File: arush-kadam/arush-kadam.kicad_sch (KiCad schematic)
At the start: 8 parts, among them IC1 AP63301WU-7

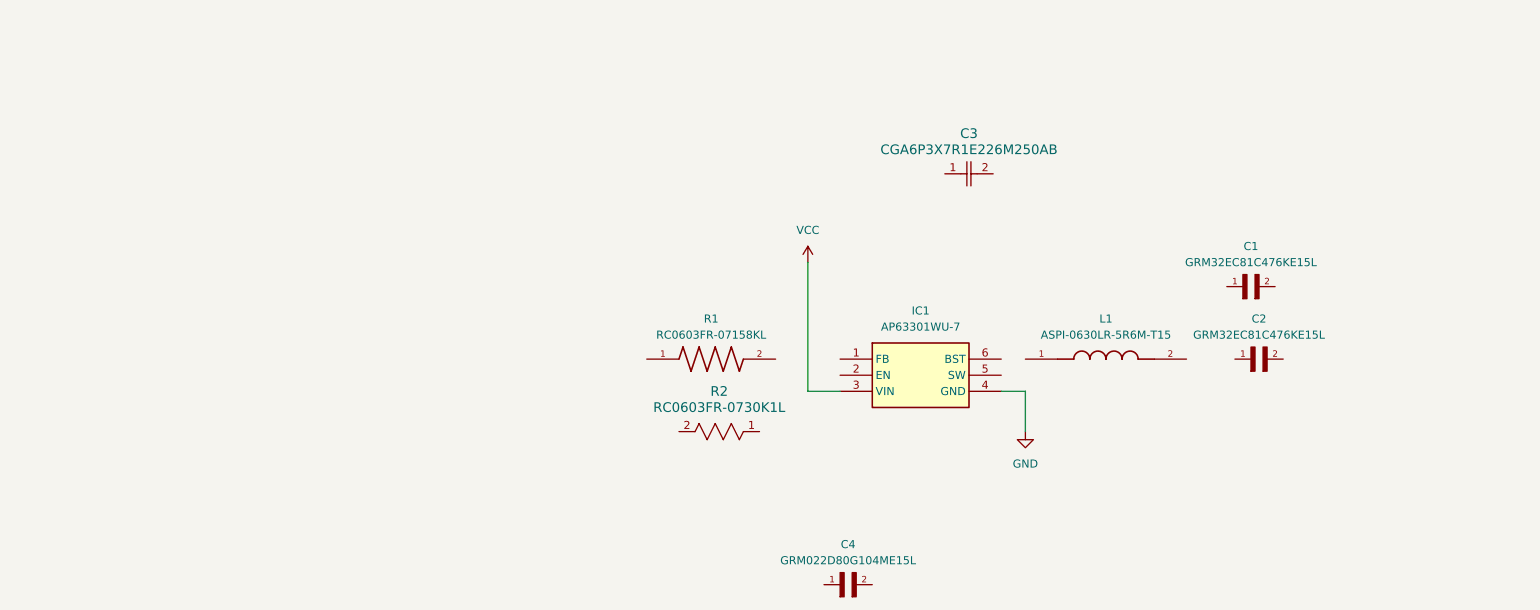
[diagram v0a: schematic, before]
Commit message: Replaced components with manufactured recommended values
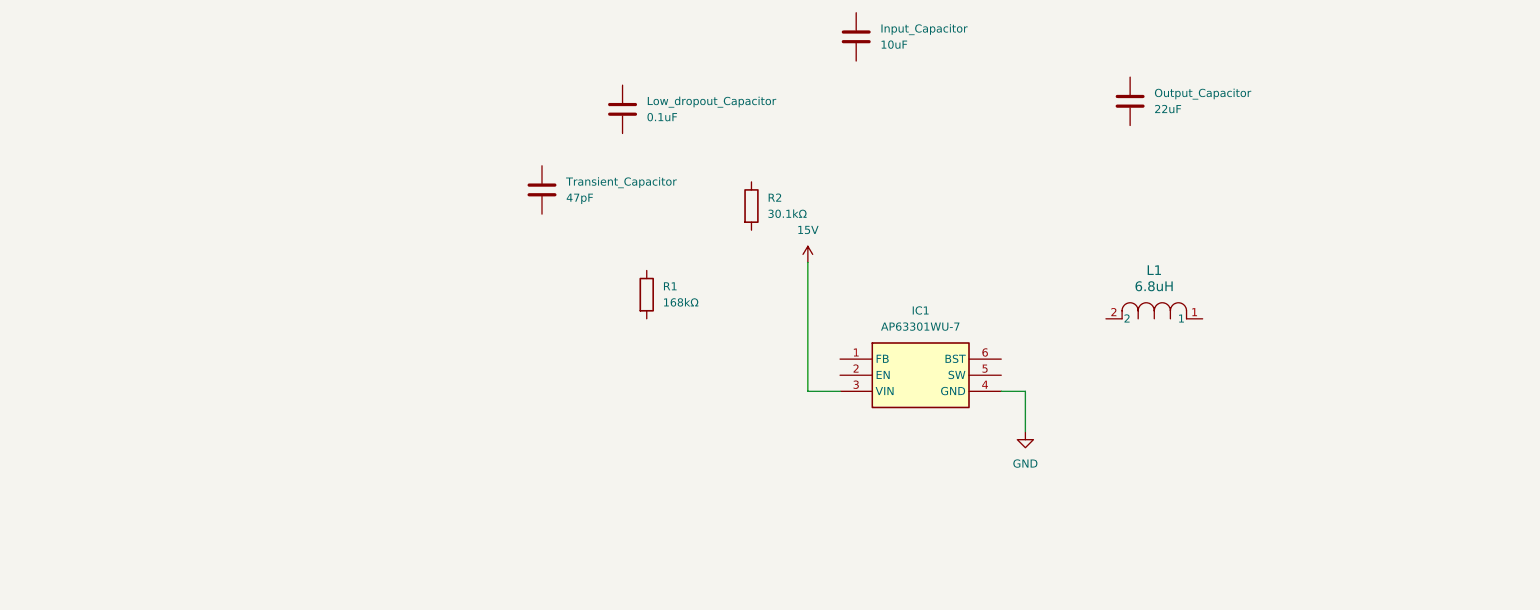
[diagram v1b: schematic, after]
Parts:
- removed C1, C2: GRM32EC81C476KE15L, GRM32EC81C476KE15L:CAPC3225X270N, symbol GRM32EC81C476KE15L:GRM32EC81C476KE15L
- removed C3: CGA6P3X7R1E226M250AB, CAP_CGA6_TDK, symbol 2026-10-15_08-26-09:CGA6P3X7R1E226M250AB
- removed C4: GRM022D80G104ME15L, GRM022D80G104ME15L:CAPC0402X22N, symbol GRM022D80G104ME15L:GRM022D80G104ME15L
- removed L1: ASPI-0630LR-5R6M-T15, ASPI-0630LR-5R6M-T15:IND_ASPI-0630LR-5R6M-T15, symbol ASPI-0630LR-5R6M-T15:ASPI-0630LR-5R6M-T15
- removed R1: RC0603FR-07158KL, RC0603FR-07158KL:RESC1608X55N, symbol RC0603FR-07158KL:RC0603FR-07158KL
- removed R2: RC0603FR-0730K1L, RC0603N_YAG, symbol 2026-10-15_00-52-59:RC0603FR-0730K1L
- added Input_Capacitor: 10uF, Capacitor_SMD:C_0805_2012Metric, symbol Device:C
- added L1: 6.8uH, IND_SRN8040TA-6R8M_BRN, symbol 2026-10-16_19-50-59:SRN8040TA-6R8M
- added Low_dropout_Capacitor: 0.1uF, Capacitor_SMD:C_0603_1608Metric_Pad1.05x0.95mm_HandSolder, symbol Device:C
- added Output_Capacitor: 22uF, Capacitor_SMD:C_0805_2012Metric, symbol Device:C
- added R1: 168kΩ, Resistor_SMD:R_0603_1608Metric_Pad0.98x0.95mm_HandSolder, symbol Device:R
- added R2: 30.1kΩ, Resistor_SMD:R_0603_1608Metric_Pad0.98x0.95mm_HandSolder, symbol Device:R
- added Transient_Capacitor: 47pF, Capacitor_SMD:C_0603_1608Metric_Pad1.05x0.95mm_HandSolder, symbol Device:C
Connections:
- net VCC renamed 15V

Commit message: Finished wiring schematic
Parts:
- removed Input_Capacitor: 10uF, Capacitor_SMD:C_0805_2012Metric, symbol Device:C
- removed Low_dropout_Capacitor: 0.1uF, Capacitor_SMD:C_0603_1608Metric_Pad1.05x0.95mm_HandSolder, symbol Device:C
- removed Output_Capacitor: 22uF, Capacitor_SMD:C_0805_2012Metric, symbol Device:C
- removed Transient_Capacitor: 47pF, Capacitor_SMD:C_0603_1608Metric_Pad1.05x0.95mm_HandSolder, symbol Device:C
- added C1 (x4): 10uF, Capacitor_SMD:C_0805_2012Metric, symbol Device:C
- added C2 (x7): 22uF, Capacitor_SMD:C_0805_2012Metric, symbol Device:C
- added C3: 0.1uF, Capacitor_SMD:C_0603_1608Metric_Pad1.05x0.95mm_HandSolder, symbol Device:C
- added C4: 47pF, Capacitor_SMD:C_0603_1608Metric_Pad1.05x0.95mm_HandSolder, symbol Device:C
- IC1: Digikey Part Number (none) -> 31-AP63301WU-7CT-ND; Digikey URL (none) -> https://www.digikey.com/en/products/detail/diodes-incorpora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
- L1: Digikey Part Number (none) -> SRN8040TA-6R8MCT-ND; Digikey URL (none) -> https://www.digikey.com/en/products/detail/bourns-inc/SRN80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; Manufacturer (none) -> Bourns Inc.
- R1: Digikey Part Number (none) -> 311-158KHRCT-ND; Digikey URL (none) -> https://www.digikey.com/en/products/detail/yageo/RC0603FR-0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; Manufacturer (none) -> YAGEO
- R2: Digikey Part Number (none) -> 311-30.1KHRCT-ND; Digikey URL (none) -> https://www.digikey.com/en/products/detail/yageo/RC0603FR-0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; Manufacturer (none) -> YAGEO
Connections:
- net 15V: now also IC1.2 (EN), C1.1, C1.1, C1.1, C1.1
- net GND: now also R2.2, C1.2, C1.2, C1.2, C1.2, C2.2, C2.2, C2.2, C2.2, C2.2, C2.2, C2.2
- net 5V: now reaches R1.1
- net 5V: now also L1.1, C2.1, C2.1, C2.1, C2.1, C2.1, C2.1, C2.1, C4.1
- net FB: now reaches R1.2
- net FB: now also IC1.1 (FB), R2.1, C4.2
- net SW: now reaches IC1.5 (SW)
- net SW: now also L1.2, C3.2
- net BST: now reaches IC1.6 (BST)
- net BST: now also C3.1

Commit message: Fixed resistor values and footprints
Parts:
- R1: value 168kΩ -> 158kΩ
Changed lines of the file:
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@@
+		)
+	)
+	(label "out"
+		(at 255.27 90.17 0)
+		(effects
+			(font
+				(size 1.27 1.27)
+			)
+			(justify left bottom)
 		)
 	)
@@
 	)
 	(label ""
+		(at 25.4 85.09 0)
+		(effects
+			(font
+				(size 1.27 1.27)
+			)
+			(justify left bottom)
+		)
+	)
+	(label "IN"
+		(at 25.4 85.09 0)
+		(effects
+			(font
+				(size 1.27 1.27)
+			)
+			(justify left bottom)
+		)
+	)
+	(label ""
 		(at 416.56 218.44 0)
 		(effects
@@
 		)
 	)
-	(label ""
-		(at 130.81 90.17 0)
+	(label "VIN"
+		(at 64.77 90.17 0)
 		(effects
 			(font
@@
 			)
 		)
-		(property "Value" "168kΩ"
+		(property "Value" "158kΩ"
 			(at 163.83 101.5999 0)
 			(show_name no)

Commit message: Added documentation PDF and fixed capacitor names on schematic
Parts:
- renumbered C2 to C10, C2 to C11, C2 to C12, C2 to C13, C1 to C2, C1 to C3, C1 to C4, C3 to C5, C4 to C6, C2 to C7, C2 to C8, C2 to C9
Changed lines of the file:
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@@
 		(in_pos_files yes)
 		(dnp no)
-		(property "Reference" "C4"
+		(property "Reference" "C6"
 			(at 142.494 100.584 0)
 			(show_name no)
@@
 			(project "arush-kadam"
 				(path "/e994741c-7c7d-4124-9d00-43b883baa61d"
-					(reference "C4")
+					(reference "C6")
 					(unit 1)
 				)
@@
 		(dnp no)
 		(fields_autoplaced yes)
-		(property "Reference" "C2"
+		(property "Reference" "C7"
 			(at 177.8 99.0599 0)
 			(show_name no)
@@
 			(project "arush-kadam"
 				(path "/e994741c-7c7d-4124-9d00-43b883baa61d"
-					(reference "C2")
+					(reference "C7")
 					(unit 1)
 				)
@@
 		(dnp no)
 		(fields_autoplaced yes)
-		(property "Reference" "C2"
+		(property "Reference" "C9"
 			(at 200.66 99.0599 0)
 			(show_name no)
@@
 			(project "arush-kadam"
 				(path "/e994741c-7c7d-4124-9d00-43b883baa61d"
-					(reference "C2")
+					(reference "C9")
 					(unit 1)
 				)
@@
 		(dnp no)
 		(fields_autoplaced yes)
-		(property "Reference" "C2"
+		(property "Reference" "C10"
 			(at 210.82 99.0599 0)
 			(show_name no)
@@
 			(project "arush-kadam"
 				(path "/e994741c-7c7d-4124-9d00-43b883baa61d"
-					(reference "C2")
+					(reference "C10")
 					(unit 1)
 				)
@@
 		(dnp no)
 		(fields_autoplaced yes)
-		(property "Reference" "C1"
+		(property "Reference" "C3"
 			(at 55.88 100.3299 0)
 			(show_name no)
@@
 			(project "arush-kadam"
 				(path "/e994741c-7c7d-4124-9d00-43b883baa61d"
-					(reference "C1")
+					(reference "C3")
 					(unit 1)
 				)
@@
 		(dnp no)
 		(fields_autoplaced yes)
-		(property "Reference" "C2"
+		(property "Reference" "C12"
 			(at 234.95 99.0599 0)
 			(show_name no)
@@
 			(project "arush-kadam"
 				(path "/e994741c-7c7d-4124-9d00-43b883baa61d"
-					(reference "C2")
+					(reference "C12")
 					(unit 1)
 				)
@@
 		(dnp no)
 		(fields_autoplaced yes)
-		(property "Reference" "C3"
+		(property "Reference" "C5"
 			(at 115.57 81.2799 0)
 			(show_name no)
@@
 			(project "arush-kadam"
 				(path "/e994741c-7c7d-4124-9d00-43b883baa61d"
-					(reference "C3")
+					(reference "C5")
 					(unit 1)
 				)
@@
 		(dnp no)
 		(fields_autoplaced yes)
-		(property "Reference" "C1"
+		(property "Reference" "C2"
 			(at 41.91 100.3299 0)
 			(show_name no)
@@
 			(project "arush-kadam"
 				(path "/e994741c-7c7d-4124-9d00-43b883baa61d"
-					(reference "C1")
+					(reference "C2")
 					(unit 1)
 				)
@@
 		(in_pos_files yes)
 		(dnp no)
-		(property "Reference" "C2"
+		(property "Reference" "C13"
 			(at 248.92 99.0599 0)
 			(show_name no)
@@
 			(project "arush-kadam"
 				(path "/e994741c-7c7d-4124-9d00-43b883baa61d"
-					(reference "C2")
+					(reference "C13")
 					(unit 1)
 				)
@@
 		(dnp no)
 		(fields_autoplaced yes)
-		(property "Reference" "C2"
+		(property "Reference" "C8"
 			(at 189.23 99.0599 0)
 			(show_name no)
@@
 			(project "arush-kadam"
 				(path "/e994741c-7c7d-4124-9d00-43b883baa61d"
-					(reference "C2")
+					(reference "C8")
 					(unit 1)
 				)
@@
 		(dnp no)
 		(fields_autoplaced yes)
-		(property "Reference" "C1"
+		(property "Reference" "C4"
 			(at 67.31 100.3299 0)
 			(show_name no)
@@
 			(project "arush-kadam"
 				(path "/e994741c-7c7d-4124-9d00-43b883baa61d"
-					(reference "C1")
+					(reference "C4")
 					(unit 1)
 				)
@@
 		(dnp no)
 		(fields_autoplaced yes)
-		(property "Reference" "C2"
+		(property "Reference" "C11"
 			(at 222.25 99.0599 0)
 			(show_name no)
@@
 			(project "arush-kadam"
 				(path "/e994741c-7c7d-4124-9d00-43b883baa61d"
-					(reference "C2")
+					(reference "C11")
 					(unit 1)
 				)
